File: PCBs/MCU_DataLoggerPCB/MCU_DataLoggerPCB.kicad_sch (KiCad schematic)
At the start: 25 parts, among them U1 24LC1025, U2 24LC1025, U3 DS1337S+, U4 ATMEGA328P-AU, Y1 Crystal, Y2 Crystal

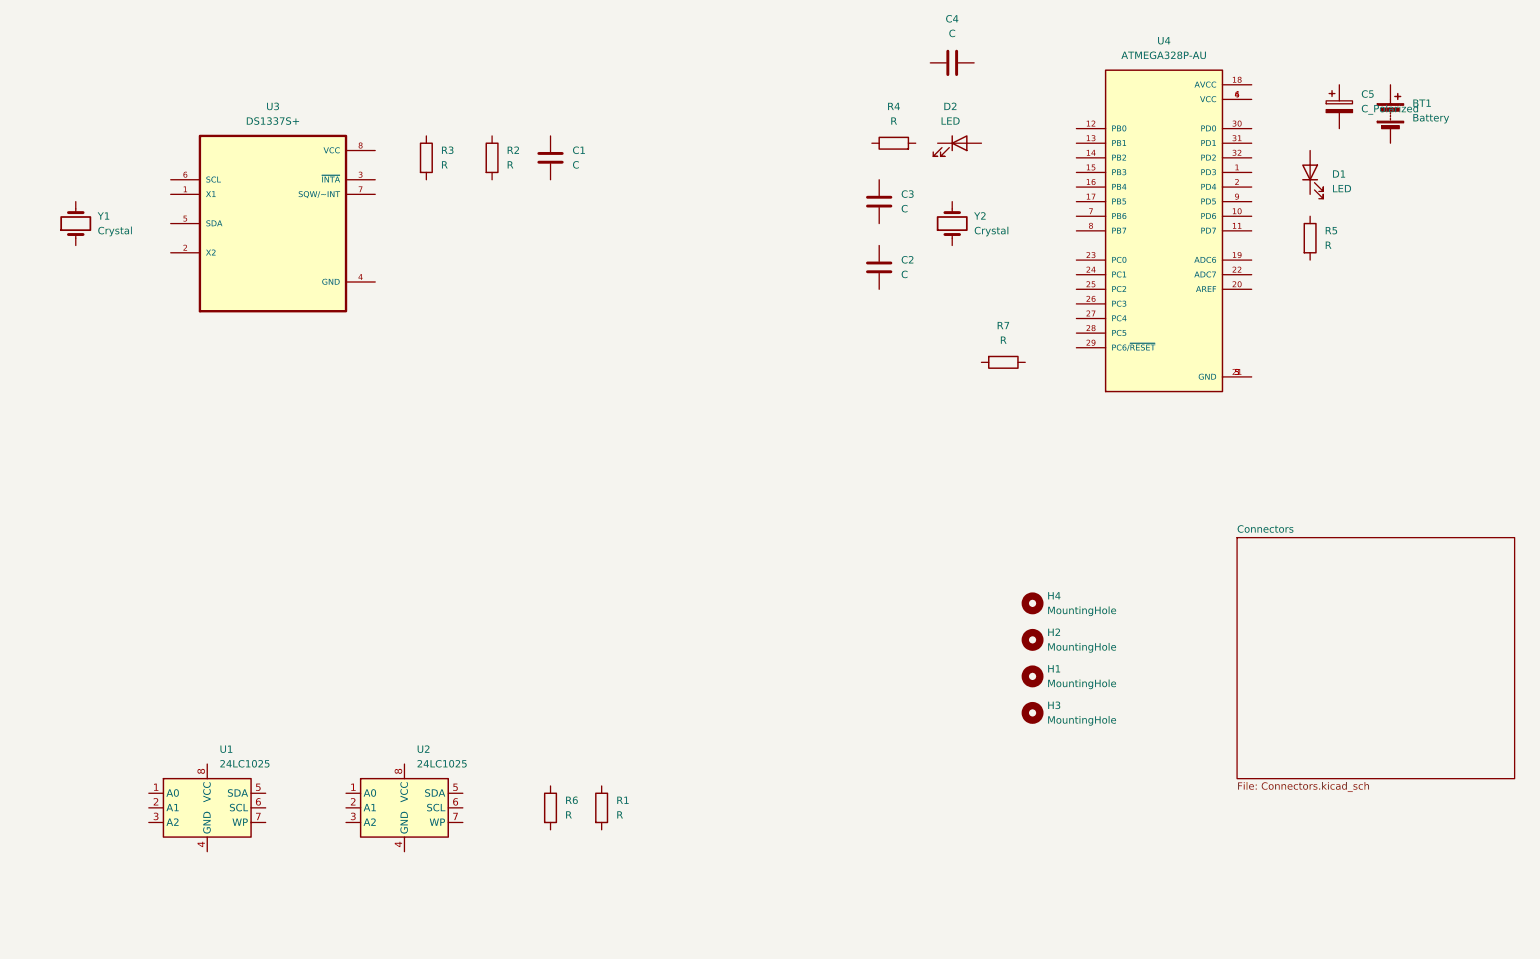
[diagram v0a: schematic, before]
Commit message: Project: add component values
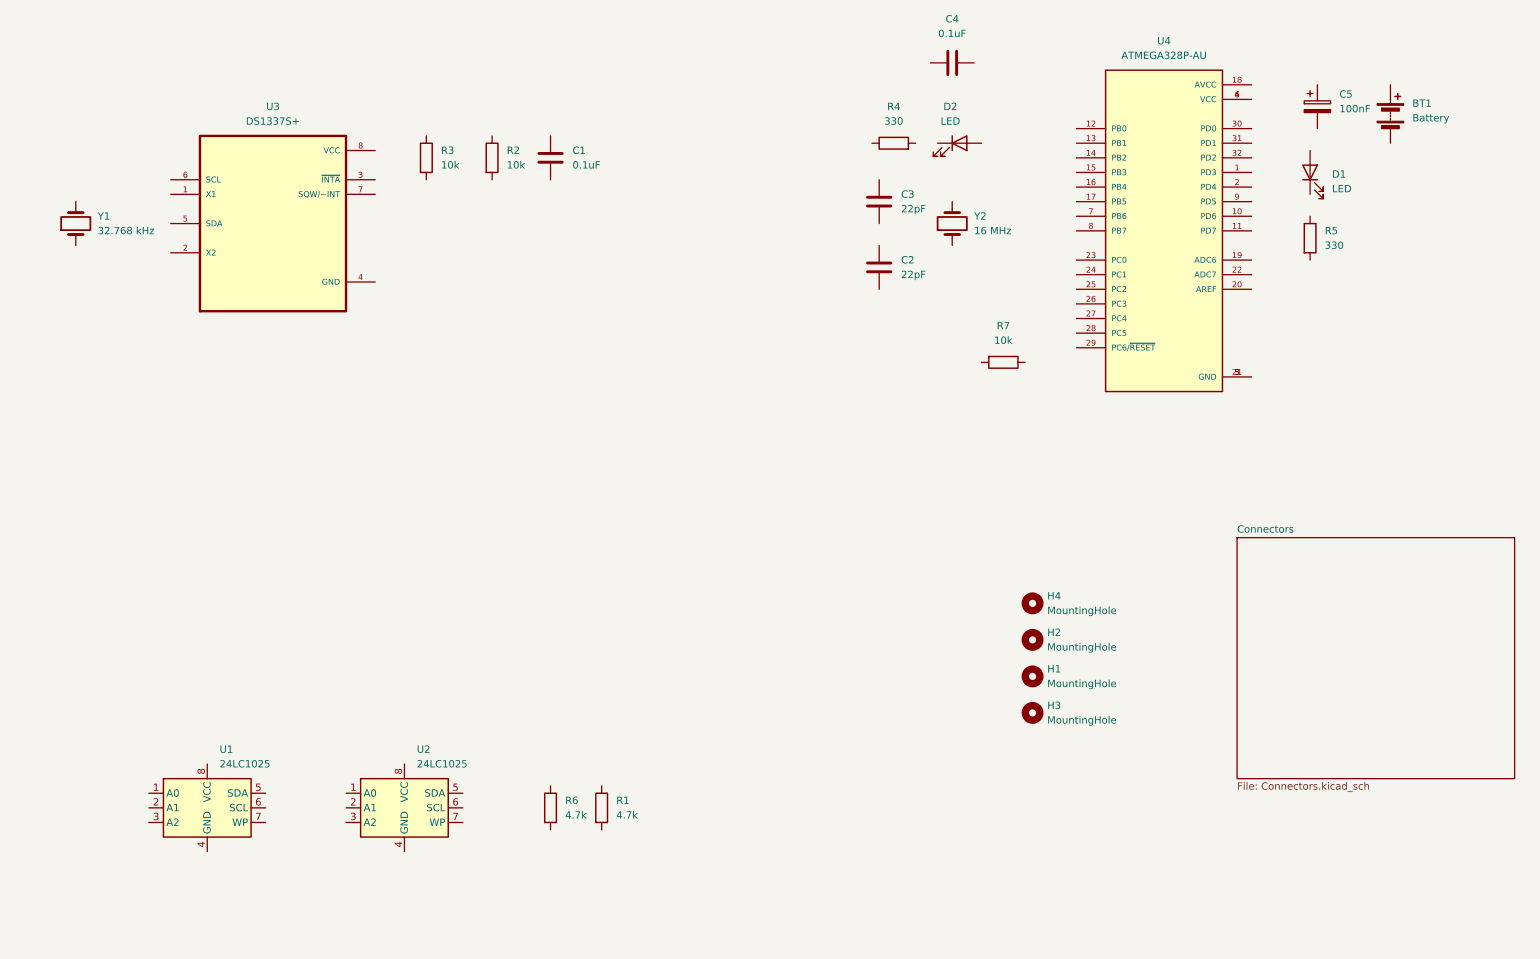
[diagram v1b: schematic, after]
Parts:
- C1, C4: value C -> 0.1uF
- C2, C3: value C -> 22pF
- C5: value C_Polarized -> 100nF
- R1, R6: value R -> 4.7k
- R2, R3, R7: value R -> 10k
- R4, R5: value R -> 330
- Y1: value Crystal -> 32.768 kHz
- Y2: value Crystal -> 16 MHz
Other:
- moved on the sheet: C5
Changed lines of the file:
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@@
 			)
 		)
-		(property "Value" "R"
+		(property "Value" "10k"
 			(at 193.04 87.63 90)
 			(effects
@@
 			)
 		)
+		(property "Purpose" ""
+			(at 193.04 91.44 0)
+			(effects
+				(font
+					(size 1.27 1.27)
+				)
+				(hide yes)
+			)
+		)
 		(pin "1"
 		)
@@
 			)
 		)
-		(property "Value" "R"
+		(property "Value" "10k"
 			(at 95.25 57.1499 0)
 			(effects
@@
 			)
 		)
+		(property "Purpose" ""
+			(at 92.71 55.88 0)
+			(effects
+				(font
+					(size 1.27 1.27)
+				)
+				(hide yes)
+			)
+		)
 		(pin "1"
 		)
@@
 			)
 		)
-		(property "Value" "R"
+		(property "Value" "10k"
 			(at 106.68 57.1499 0)
 			(effects
@@
 			)
 		)
+		(property "Purpose" ""
+			(at 104.14 55.88 0)
+			(effects
+				(font
+					(size 1.27 1.27)
+				)
+				(hide yes)
+			)
+		)
 		(pin "1"
 		)
@@
 			)
 		)
-		(property "Value" "C"
+		(property "Value" "22pF"
 			(at 175.26 64.7699 0)
 			(effects
@@
 			)
 		)
+		(property "Purpose" ""
+			(at 171.45 63.5 0)
+			(effects
+				(font
+					(size 1.27 1.27)
+				)
+				(hide yes)
+			)
+		)
 		(pin "1"
 		)
@@
 			)
 		)
-		(property "Value" "C"
+		(property "Value" "22pF"
 			(at 175.26 76.1999 0)
 			(effects
@@
 			)
 		)
+		(property "Purpose" ""
+			(at 171.45 74.93 0)
+			(effects
+				(font
+					(size 1.27 1.27)
+				)
+				(hide yes)
+			)
+		)
 		(pin "1"
 		)
@@
 			)
 		)
-		(property "Value" "Crystal"
+		(property "Value" "16 MHz"
 			(at 187.96 68.5799 90)
 			(effects
@@
 			)
 		)
+		(property "Purpose" ""
+			(at 184.15 67.31 0)
+			(effects
+				(font
+					(size 1.27 1.27)
+				)
+				(hide yes)
+			)
+		)
 		(pin "1"
 		)
@@
 			)
 		)
-		(property "Value" "R"
+		(property "Value" "4.7k"
 			(at 116.84 170.1799 0)
 			(effects
@@
 			)
 		)
+		(property "Purpose" ""
+			(at 114.3 168.91 0)
+			(effects
+				(font
+					(size 1.27 1.27)
+				)
+				(hide yes)
+			)
+		)
 		(pin "1"
 		)
@@
 			)
 		)
-		(property "Value" "C"
+		(property "Value" "0.1uF"
 			(at 118.11 57.1499 0)
 			(effects
@@
 			)
 		)
+		(property "Purpose" ""
+			(at 114.3 55.88 0)
+			(effects
+				(font
+					(size 1.27 1.27)
+				)
+				(hide yes)
+			)
+		)
 		(pin "1"
 		)
@@
 	(symbol
 		(lib_id "Device:C_Polarized")
-		(at 251.46 46.99 0)
+		(at 247.65 46.99 0)
 		(unit 1)
 		(exclude_from_sim no)
@@
 		(fields_autoplaced yes)
 		(property "Reference" "C5"
-			(at 255.27 44.8309 0)
-			(effects
-				(font
-					(size 1.27 1.27)
-				)
-				(justify left)
-			)
-		)
-		(property "Value" "C_Polarized"
-			(at 255.27 47.3709 0)
-			(effects
-				(font
-					(size 1.27 1.27)
-				)
-				(justify left)
-			)
-		)
-		(property "Footprint" ""
-			(at 252.4252 50.8 0)
+			(at 251.46 44.8309 0)
+			(effects
+				(font
+					(size 1.27 1.27)
+				)
+				(justify left)
+			)
+		)
+		(property "Value" "100nF"
+			(at 251.46 47.3709 0)
+			(effects
+				(font
+					(size 1.27 1.27)
+				)
+				(justify left)
+			)
+		)
+		(property "Footprint" ""
+			(at 248.6152 50.8 0)
 			(effects
 				(font
@@
 		)
 		(property "Datasheet" "~"
-			(at 251.46 46.99 0)
+			(at 247.65 46.99 0)
 			(effects
 				(font
@@
 		)
 		(property "Description" "Polarized capacitor"
-			(at 251.46 46.99 0)
+			(at 247.65 46.99 0)
+			(effects
+				(font
+					(size 1.27 1.27)
+				)
+				(hide yes)
+			)
+		)
+		(property "Purpose" ""
+			(at 247.65 46.99 0)
 			(effects
 				(font
@@
 			)
 		)
-		(property "Value" "C"
+		(property "Value" "0.1uF"
 			(at 184.15 34.29 90)
 			(effects
@@
 			)
 		)
+		(property "Purpose" ""
+			(at 184.15 39.37 0)
+			(effects
+				(font
+					(size 1.27 1.27)
+				)
+				(hide yes)
+			)
+		)
 		(pin "1"
 		)
@@
 			)
 		)
-		(property "Value" "Crystal"
+		(property "Value" "32.768 kHz"
 			(at 35.56 68.5799 90)
 			(effects
@@
 			)
 		)
+		(property "Purpose" ""
+			(at 31.75 67.31 0)
+			(effects
+				(font
+					(size 1.27 1.27)
+				)
+				(hide yes)
+			)
+		)
 		(pin "2"
 		)
@@
 			)
 		)
-		(property "Value" "R"
+		(property "Value" "4.7k"
 			(at 125.73 170.1799 0)
 			(effects
@@
 			)
 		)
+		(property "Purpose" ""
+			(at 123.19 168.91 0)
+			(effects
+				(font
+					(size 1.27 1.27)
+				)
+				(hide yes)
+			)
+		)
 		(pin "1"
 		)
@@
 			)
 		)
-		(property "Value" "R"
+		(property "Value" "330"
 			(at 173.99 49.53 90)
 			(effects
@@
 			)
 		)
+		(property "Purpose" ""
+			(at 173.99 53.34 0)
+			(effects
+				(font
+					(size 1.27 1.27)
+				)
+				(hide yes)
+			)
+		)
 		(pin "1"
 		)
@@
 			)
 		)
-		(property "Value" "R"
+		(property "Value" "330"
 			(at 248.92 71.1199 0)
 			(effects
@@
 			(at 246.38 69.85 0)
 			(effects
+				(font
+					(size 1.27 1.27)
+				)
+				(hide yes)
+			)
+		)
+		(property "Purpose" ""
+			(at 246.38 69.85 0)
+			(effects

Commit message: Project: completed symbol-footprint associations
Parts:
- BT1: footprint (none) -> Connector_PinHeader_2.54mm:PinHeader_1x02_P2.54mm_Vertical
- C1, C2, C3, C4, C5: footprint (none) -> Capacitor_SMD:C_0805_2012Metric_Pad1.18x1.45mm_HandSolder
- D1, D2: footprint (none) -> LED_SMD:LED_0805_2012Metric_Pad1.15x1.40mm_HandSolder
- H1, H2, H3, H4: footprint (none) -> MountingHole:MountingHole_2.2mm_M2
- R1, R2, R3, R4, R5, R6, R7: footprint (none) -> Resistor_SMD:R_0805_2012Metric_Pad1.20x1.40mm_HandSolder
- U1, U2: footprint (none) -> Package_SO:SOIC-8_5.3x5.3mm_P1.27mm
- U3: footprint DS1337S_:SOIC127P600X175-8N -> Footprints:SOIC127P600X175-8N
- U4: footprint ATMEGA328P-AU:QFP80P900X900X120-32N -> Footprints:QFP80P900X900X120-32N
- Y1, Y2: footprint (none) -> Crystal:Crystal_SMD_5032-2Pin_5.0x3.2mm_HandSoldering
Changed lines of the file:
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@@
 			)
 		)
-		(property "Footprint" ""
+		(property "Footprint" "Resistor_SMD:R_0805_2012Metric_Pad1.20x1.40mm_HandSolder"
 			(at 193.04 89.662 90)
 			(effects
@@
 			)
 		)
-		(property "Footprint" ""
+		(property "Footprint" "Resistor_SMD:R_0805_2012Metric_Pad1.20x1.40mm_HandSolder"
 			(at 90.932 55.88 90)
 			(effects
@@
 			)
 		)
-		(property "Footprint" "DS1337S_:SOIC127P600X175-8N"
+		(property "Footprint" "Footprints:SOIC127P600X175-8N"
 			(at 66.04 67.31 0)
 			(effects
@@
 			)
 		)
-		(property "Footprint" ""
+		(property "Footprint" "Resistor_SMD:R_0805_2012Metric_Pad1.20x1.40mm_HandSolder"
 			(at 102.362 55.88 90)
 			(effects
@@
 			)
 		)
-		(property "Footprint" ""
+		(property "Footprint" "Capacitor_SMD:C_0805_2012Metric_Pad1.18x1.45mm_HandSolder"
 			(at 172.4152 67.31 0)
 			(effects
@@
 			)
 		)
-		(property "Footprint" ""
+		(property "Footprint" "Capacitor_SMD:C_0805_2012Metric_Pad1.18x1.45mm_HandSolder"
 			(at 172.4152 78.74 0)
 			(effects
@@
 			)
 		)
-		(property "Footprint" ""
+		(property "Footprint" "MountingHole:MountingHole_2.2mm_M2"
 			(at 198.12 146.05 0)
 			(effects
@@
 			)
 		)
-		(property "Footprint" ""
+		(property "Footprint" "MountingHole:MountingHole_2.2mm_M2"
 			(at 198.12 152.4 0)
 			(effects
@@
 			)
 		)
-		(property "Footprint" ""
+		(property "Footprint" "Crystal:Crystal_SMD_5032-2Pin_5.0x3.2mm_HandSoldering"
 			(at 184.15 67.31 0)
 			(effects
@@
 			)
 		)
-		(property "Footprint" ""
+		(property "Footprint" "Resistor_SMD:R_0805_2012Metric_Pad1.20x1.40mm_HandSolder"
 			(at 112.522 168.91 90)
 			(effects
@@
 			)
 		)
-		(property "Footprint" ""
+		(property "Footprint" "LED_SMD:LED_0805_2012Metric_Pad1.15x1.40mm_HandSolder"
 			(at 246.38 58.42 0)
 			(effects
@@
 			)
 		)
-		(property "Footprint" ""
+		(property "Footprint" "Package_SO:SOIC-8_5.3x5.3mm_P1.27mm"
 			(at 54.61 168.91 0)
 			(effects
@@
 			)
 		)
-		(property "Footprint" "ATMEGA328P-AU:QFP80P900X900X120-32N"
+		(property "Footprint" "Footprints:QFP80P900X900X120-32N"
 			(at 220.98 68.58 0)
 			(effects
@@
 			)
 		)
-		(property "Footprint" ""
+		(property "Footprint" "Capacitor_SMD:C_0805_2012Metric_Pad1.18x1.45mm_HandSolder"
 			(at 115.2652 59.69 0)
 			(effects
@@
 			)
 		)
-		(property "Footprint" ""
+		(property "Footprint" "Capacitor_SMD:C_0805_2012Metric_Pad1.18x1.45mm_HandSolder"
 			(at 248.6152 50.8 0)
 			(effects
@@
 			)
 		)
-		(property "Footprint" ""
+		(property "Footprint" "Capacitor_SMD:C_0805_2012Metric_Pad1.18x1.45mm_HandSolder"
 			(at 187.96 38.4048 0)
 			(effects
@@
 			)
 		)
-		(property "Footprint" ""
+		(property "Footprint" "Crystal:Crystal_SMD_5032-2Pin_5.0x3.2mm_HandSoldering"
 			(at 31.75 67.31 0)
 			(effects
@@
 			)
 		)
-		(property "Footprint" ""
+		(property "Footprint" "Connector_PinHeader_2.54mm:PinHeader_1x02_P2.54mm_Vertical"
 			(at 260.35 46.736 90)
 			(effects
@@
 			)
 		)
-		(property "Footprint" ""
+		(property "Footprint" "Package_SO:SOIC-8_5.3x5.3mm_P1.27mm"
 			(at 88.9 168.91 0)
 			(effects
@@
 			)
 		)
-		(property "Footprint" ""
+		(property "Footprint" "Resistor_SMD:R_0805_2012Metric_Pad1.20x1.40mm_HandSolder"
 			(at 121.412 168.91 90)
 			(effects
@@
 			)
 		)
-		(property "Footprint" ""
+		(property "Footprint" "LED_SMD:LED_0805_2012Metric_Pad1.15x1.40mm_HandSolder"
 			(at 185.42 53.34 0)
 			(effects
@@
 			)
 		)
-		(property "Footprint" ""
+		(property "Footprint" "Resistor_SMD:R_0805_2012Metric_Pad1.20x1.40mm_HandSolder"
 			(at 173.99 55.118 90)
 			(effects
@@
 			)
 		)
-		(property "Footprint" ""
+		(property "Footprint" "MountingHole:MountingHole_2.2mm_M2"
 			(at 198.12 133.35 0)
 			(effects
@@
 			)
 		)
-		(property "Footprint" ""
+		(property "Footprint" "MountingHole:MountingHole_2.2mm_M2"
 			(at 198.12 139.7 0)
 			(effects
@@
 			)
 		)
-		(property "Footprint" ""
+		(property "Footprint" "Resistor_SMD:R_0805_2012Metric_Pad1.20x1.40mm_HandSolder"
 			(at 244.602 69.85 90)
 			(effects
